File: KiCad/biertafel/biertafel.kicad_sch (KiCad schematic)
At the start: 28 parts, among them J1 Screw_Terminal_01x02, J10 Screw_Terminal_01x02, J11 Conn_01x20_Socket, J2 Screw_Terminal_01x02, J3 Screw_Terminal_01x02, J4 Screw_Terminal_01x02, J5 Screw_Terminal_01x02, J6 Screw_Terminal_01x02, J7 Screw_Terminal_01x02, J8 Screw_Terminal_01x02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

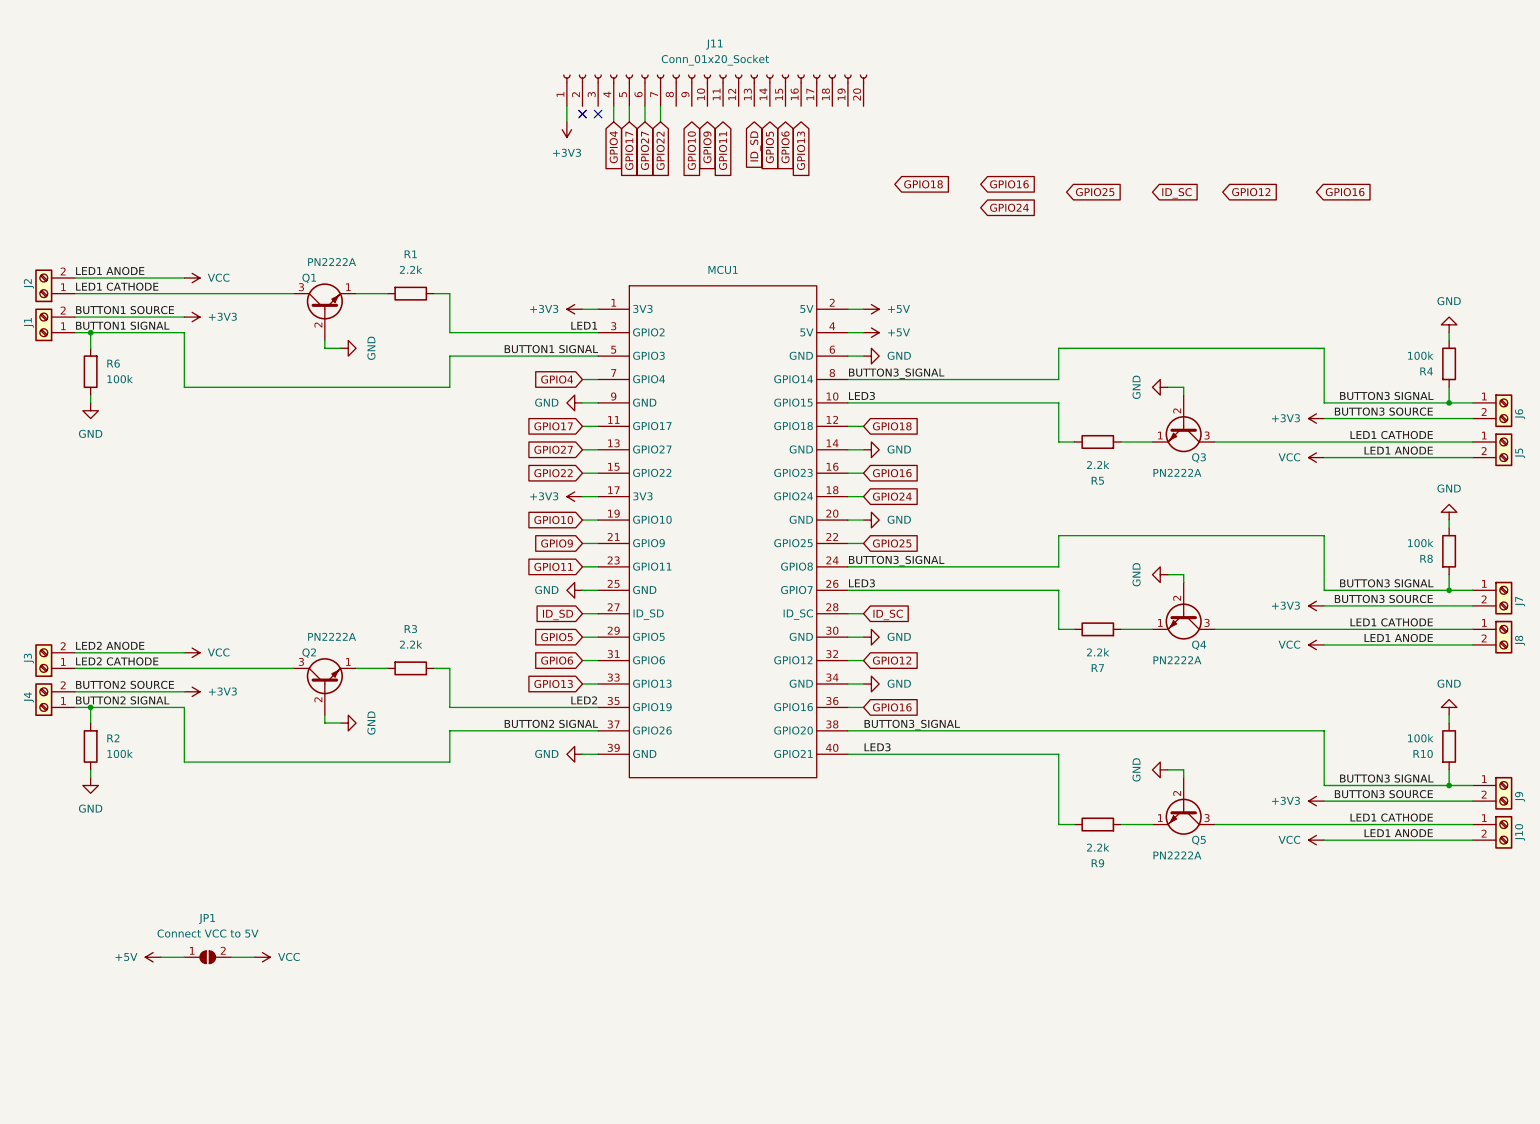
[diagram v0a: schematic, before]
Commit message: Raspberry PI Zero W symbol now contains all functionalities per port
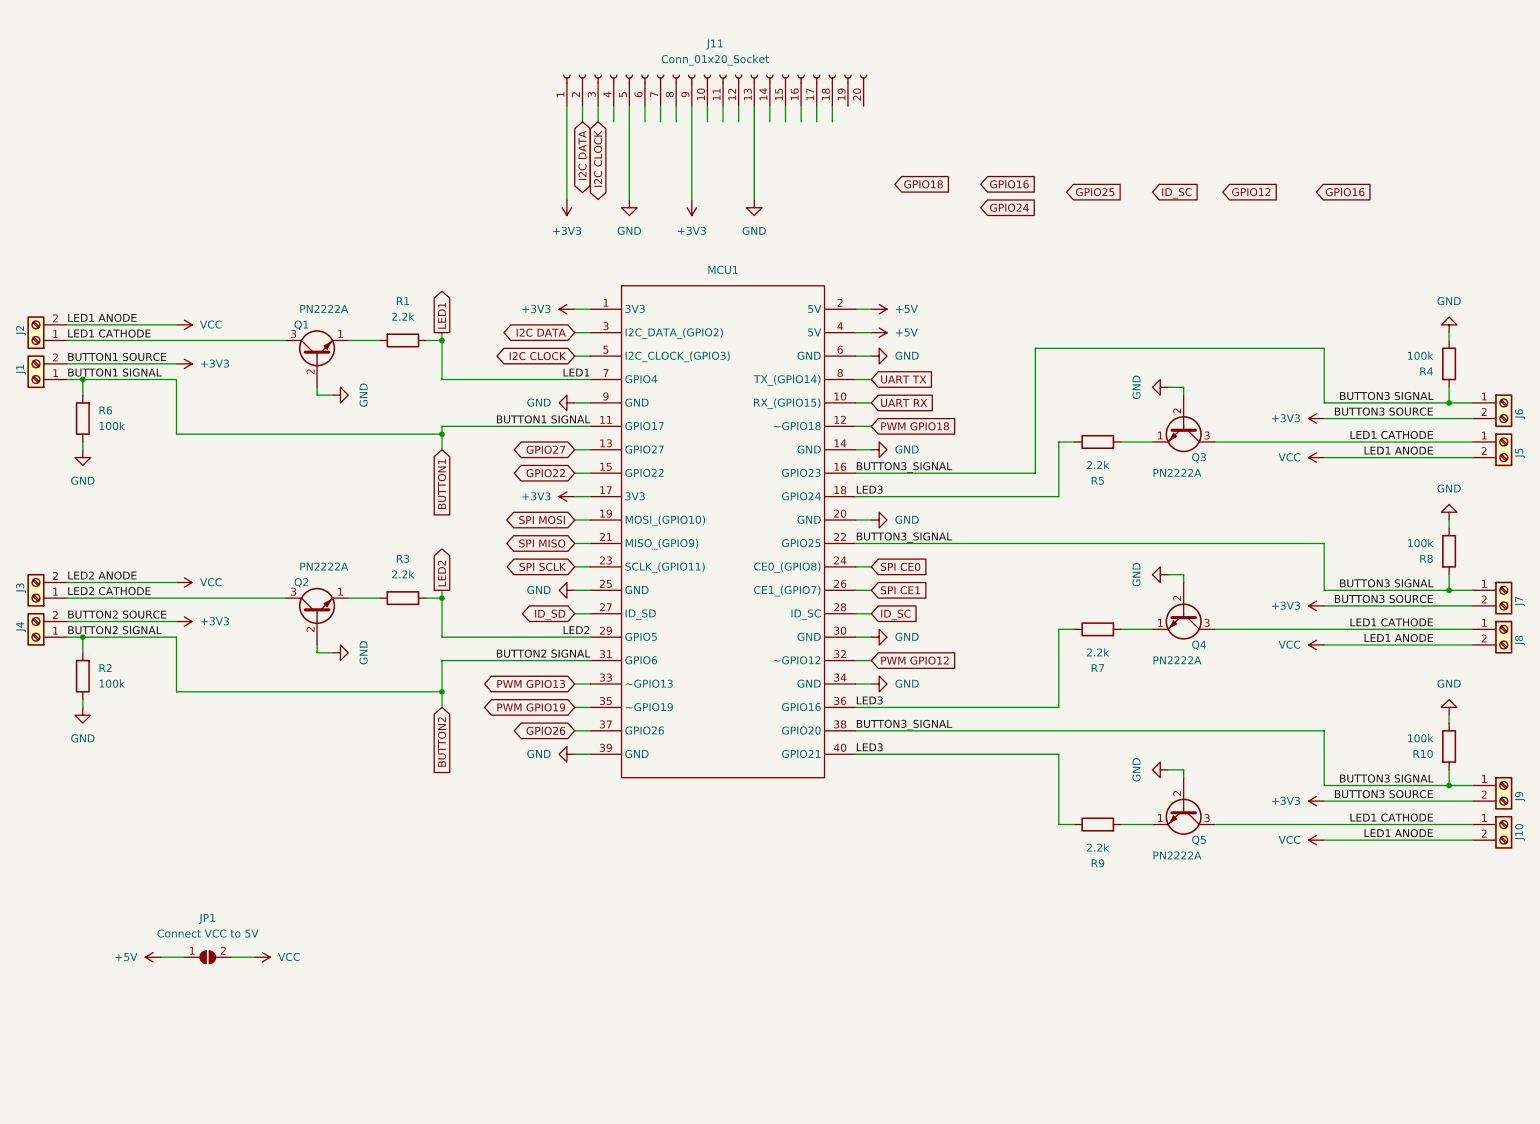
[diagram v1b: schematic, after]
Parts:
- removed MCU1: ~, symbol eigen_symbolen:Raspberry_Pi_zero_W
- added MCU1: ~, symbol biertafel:Raspberry_PI_Zero_W
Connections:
- net GPIO17 is gone; now on net GND: J11.5 (Pin_5)
- net +3V3: now also J11.9 (Pin_9), MCU1.1 (3V3), MCU1.17 (3V3)
- net +5V: now also MCU1.2 (5V), MCU1.4 (5V)
- net BUTTON3 SIGNAL: now also MCU1.16 (GPIO23), MCU1.22 (GPIO25), MCU1.38 (GPIO20)
- net GND: now also J11.13 (Pin_13), MCU1.14 (GND), MCU1.20 (GND), MCU1.25 (GND), MCU1.30 (GND), MCU1.34 (GND), MCU1.39 (GND), MCU1.6 (GND), MCU1.9 (GND)
- net GPIO22: now also MCU1.15 (GPIO22); no longer J11.7 (Pin_7)
- net GPIO27: now also MCU1.13 (GPIO27); no longer J11.6 (Pin_6)
- net ID_SC: now also MCU1.28 (ID_SC)
- net ID_SD: now also MCU1.27 (ID_SD)
- net LED1: now also MCU1.7 (GPIO4)
- net LED2: now also MCU1.29 (GPIO5)
- net LED3: now also MCU1.18 (GPIO24), MCU1.36 (GPIO16), MCU1.40 (GPIO21)
- net I2C DATA: now reaches J11.2 (Pin_2)
- net I2C DATA: now also MCU1.3 (I2C_DATA_(GPIO2))
- net I2C CLOCK: now reaches J11.3 (Pin_3)
- net I2C CLOCK: now also MCU1.5 (I2C_CLOCK_(GPIO3))
- net BUTTON1 SIGNAL renamed BUTTON1
- net BUTTON1: now also MCU1.11 (GPIO17)
- net BUTTON2 SIGNAL renamed BUTTON2
- net BUTTON2: now also MCU1.31 (GPIO6)
- net GPIO4: no longer names the net of J11.4 (Pin_4)
- new net GPIO26: MCU1.37 (GPIO26)
- new net PWM GPIO12: MCU1.32 (~GPIO12)
- new net PWM GPIO13: MCU1.33 (~GPIO13)
- new net PWM GPIO18: MCU1.12 (~GPIO18)
- new net PWM GPIO19: MCU1.35 (~GPIO19)
- new net SPI CE0: MCU1.24 (CE0_(GPIO8))
- new net SPI CE1: MCU1.26 (CE1_(GPIO7))
- new net SPI MISO: MCU1.21 (MISO_(GPIO9))
- new net SPI MOSI: MCU1.19 (MOSI_(GPIO10))
- new net SPI SCLK: MCU1.23 (SCLK_(GPIO11))
- new net UART RX: MCU1.10 (RX_(GPIO15))
- new net UART TX: MCU1.8 (TX_(GPIO14))
- no-connect marks 2 -> 0
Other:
- moved on the sheet: J1, J2, J3, J4, Q1, Q2, R1, R2, R3, R6

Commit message: First version of schematic finished, started with PCB layout
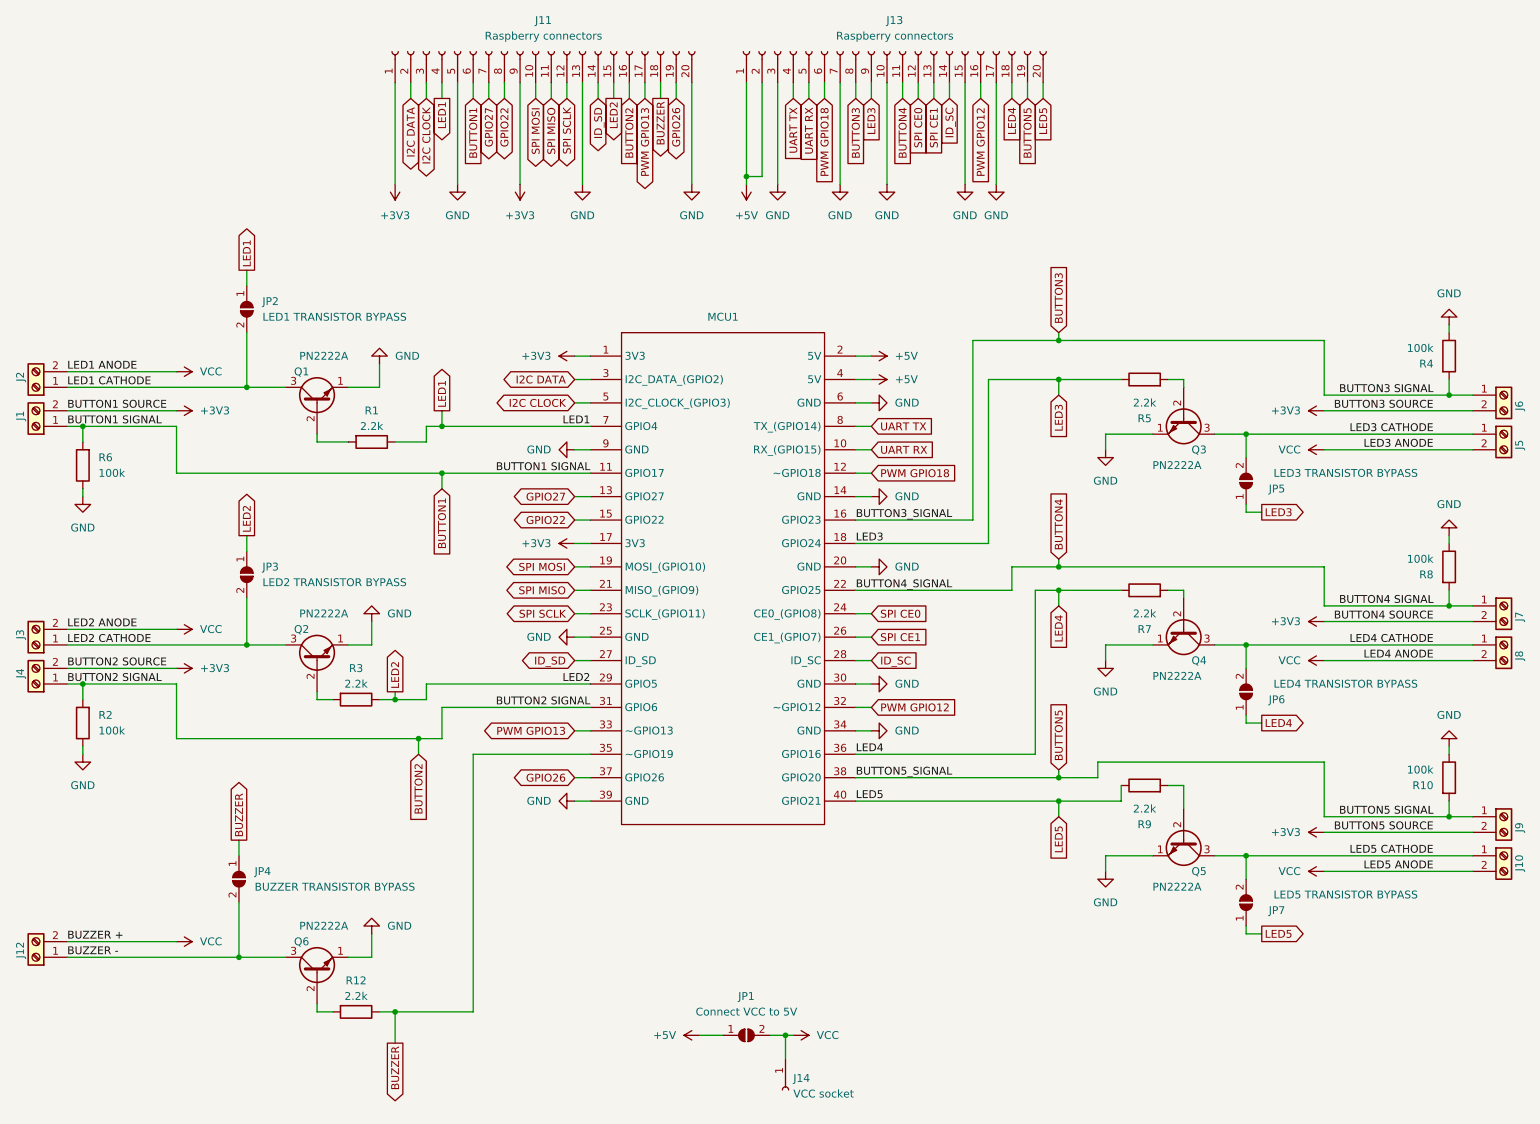
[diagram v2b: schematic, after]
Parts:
- added J12: Screw_Terminal_01x02, SamacSys_Parts:1725656, symbol Connector:Screw_Terminal_01x02
- added J13: Raspberry connectors, Connector_PinSocket_2.54mm:PinSocket_1x20_P2.54mm_Vertical, symbol Connector:Conn_01x20_Socket
- added J14: VCC socket, Connector_PinSocket_2.54mm:PinSocket_1x01_P2.54mm_Vertical, symbol Connector:Conn_01x01_Socket
- added JP2: LED1 TRANSISTOR BYPASS, Jumper:SolderJumper-2_P1.3mm_Open_RoundedPad1.0x1.5mm, symbol Jumper:SolderJumper_2_Open
- added JP3: LED2 TRANSISTOR BYPASS, Jumper:SolderJumper-2_P1.3mm_Open_RoundedPad1.0x1.5mm, symbol Jumper:SolderJumper_2_Open
- added JP4: BUZZER TRANSISTOR BYPASS, Jumper:SolderJumper-2_P1.3mm_Open_RoundedPad1.0x1.5mm, symbol Jumper:SolderJumper_2_Open
- added JP5: LED3 TRANSISTOR BYPASS, Jumper:SolderJumper-2_P1.3mm_Open_RoundedPad1.0x1.5mm, symbol Jumper:SolderJumper_2_Open
- added JP6: LED4 TRANSISTOR BYPASS, Jumper:SolderJumper-2_P1.3mm_Open_RoundedPad1.0x1.5mm, symbol Jumper:SolderJumper_2_Open
- added JP7: LED5 TRANSISTOR BYPASS, Jumper:SolderJumper-2_P1.3mm_Open_RoundedPad1.0x1.5mm, symbol Jumper:SolderJumper_2_Open
- added Q6: PN2222A, Package_TO_SOT_THT:TO-92_Inline, symbol Transistor_BJT:PN2222A
- added R12: 2.2k, Resistor_THT:R_Axial_DIN0207_L6.3mm_D2.5mm_P10.16mm_Horizontal, symbol Device:R
- J1, J10, J2, J3, J4, J5, J6, J7, J8, J9: footprint (none) -> SamacSys_Parts:1725656
- J11: value Conn_01x20_Socket -> Raspberry connectors; footprint (none) -> Connector_PinSocket_2.54mm:PinSocket_1x20_P2.54mm_Vertical
- JP1: footprint (none) -> Jumper:SolderJumper-2_P1.3mm_Open_RoundedPad1.0x1.5mm
- MCU1: footprint (none) -> biertafel:Raspberry PI Zero W
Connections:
- net PWM GPIO19 is gone; now on net BUZZER: MCU1.35 (~GPIO19)
- net +5V: now also J13.1 (Pin_1), J13.2 (Pin_2)
- net BUTTON1: now also J11.6 (Pin_6)
- net BUTTON2: now also J11.16 (Pin_16)
- net GND: now also J11.20 (Pin_20), Q1.1 (E), Q2.1 (E), Q3.1 (E), Q4.1 (E), Q5.1 (E), J13.10 (Pin_10), J13.15 (Pin_15), J13.17 (Pin_17), J13.3 (Pin_3), J13.7 (Pin_7), Q6.1 (E); no longer Q1.2 (B), Q2.2 (B), Q3.2 (B), Q4.2 (B), Q5.2 (B)
- net GPIO22: now also J11.8 (Pin_8)
- net GPIO26: now also J11.19 (Pin_19)
- net GPIO27: now also J11.7 (Pin_7)
- net ID_SC: now also J13.14 (Pin_14)
- net ID_SD: now also J11.14 (Pin_14)
- net LED1: now also J11.4 (Pin_4), JP2.1 (A)
- net LED1 CATHODE: now also JP2.2 (B); no longer J10.1 (Pin_1), J5.1 (Pin_1), J8.1 (Pin_1), Q3.3 (C), Q4.3 (C), Q5.3 (C)
- net LED2: now also J11.15 (Pin_15), JP3.1 (A)
- net LED2 CATHODE: now also JP3.2 (B)
- net LED3: now also J13.9 (Pin_9), JP5.1 (A); no longer MCU1.36 (GPIO16), MCU1.40 (GPIO21), R7.1, R9.1
- net PWM GPIO12: now also J13.16 (Pin_16)
- net PWM GPIO13: now also J11.17 (Pin_17)
- net PWM GPIO18: now also J13.6 (Pin_6)
- net SPI CE0: now also J13.12 (Pin_12)
- net SPI CE1: now also J13.13 (Pin_13)
- net SPI MISO: now also J11.11 (Pin_11)
- net SPI MOSI: now also J11.10 (Pin_10)
- net SPI SCLK: now also J11.12 (Pin_12)
- net UART RX: now also J13.5 (Pin_5)
- net UART TX: now also J13.4 (Pin_4)
- net VCC: now also J12.2 (Pin_2), J14.1 (Pin_1)
- net at R1.2: now also Q1.2 (B); no longer Q1.1 (E)
- net at R9.2: now also Q5.2 (B); no longer Q5.1 (E)
- net at R7.2: now also Q4.2 (B); no longer Q4.1 (E)
- net BUZZER: now reaches J11.18 (Pin_18)
- net BUZZER: now also JP4.1 (A), R12.1
- net at R3.2: now also Q2.2 (B); no longer Q2.1 (E)
- net at R5.2: now also Q3.2 (B); no longer Q3.1 (E)
- removed net BUTTON3 SIGNAL: J6.1 (Pin_1), J7.1 (Pin_1), J9.1 (Pin_1), MCU1.16 (GPIO23), MCU1.22 (GPIO25), MCU1.38 (GPIO20), R10.2, R4.2, R8.2
- new net: Q6.2 (B), R12.2
- new net BUTTON3: J13.8 (Pin_8), J6.1 (Pin_1), MCU1.16 (GPIO23), R4.2
- new net BUTTON4: J13.11 (Pin_11), J7.1 (Pin_1), MCU1.22 (GPIO25), R8.2
- new net BUTTON5: J13.19 (Pin_19), J9.1 (Pin_1), MCU1.38 (GPIO20), R10.2
- new net BUZZER -: J12.1 (Pin_1), JP4.2 (B), Q6.3 (C)
- new net LED3 CATHODE: J5.1 (Pin_1), JP5.2 (B), Q3.3 (C)
- new net LED4: J13.18 (Pin_18), JP6.1 (A), MCU1.36 (GPIO16), R7.1
- new net LED4 CATHODE: J8.1 (Pin_1), JP6.2 (B), Q4.3 (C)
- new net LED5: J13.20 (Pin_20), JP7.1 (A), MCU1.40 (GPIO21), R9.1
- new net LED5 CATHODE: J10.1 (Pin_1), JP7.2 (B), Q5.3 (C)
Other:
- company: (none) -> Piri piri b.v.
- title: (none) -> Game table
- moved on the sheet: J1, J10, J11, J2, J3, J4, J5, J6, J7, J8, J9, JP1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
